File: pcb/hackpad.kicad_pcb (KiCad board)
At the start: 2 copper layers, 83.3 x 61.9 mm, 32 parts, among them U1 XIAO-RP2040-SMD

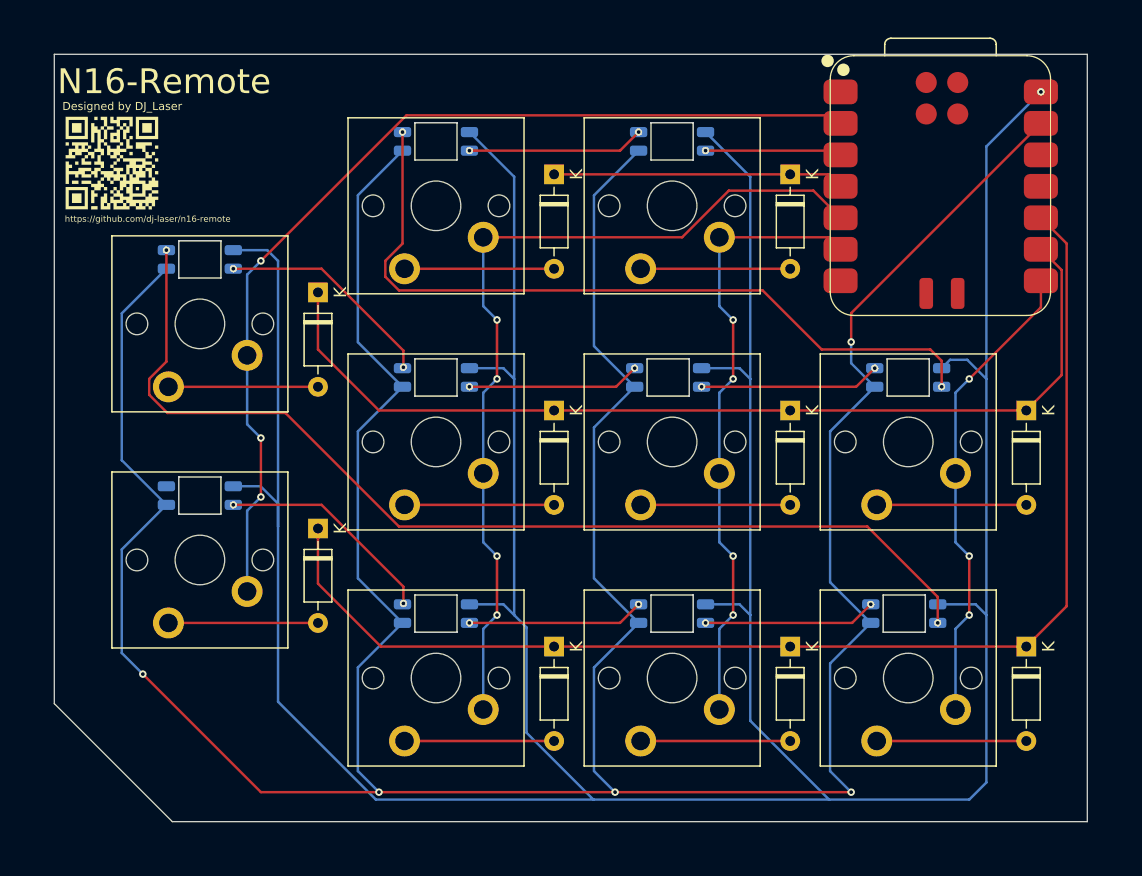
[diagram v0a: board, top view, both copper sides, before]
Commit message: i used the wrong data sheet to edit the footprint, changed the pcb to actually work :(
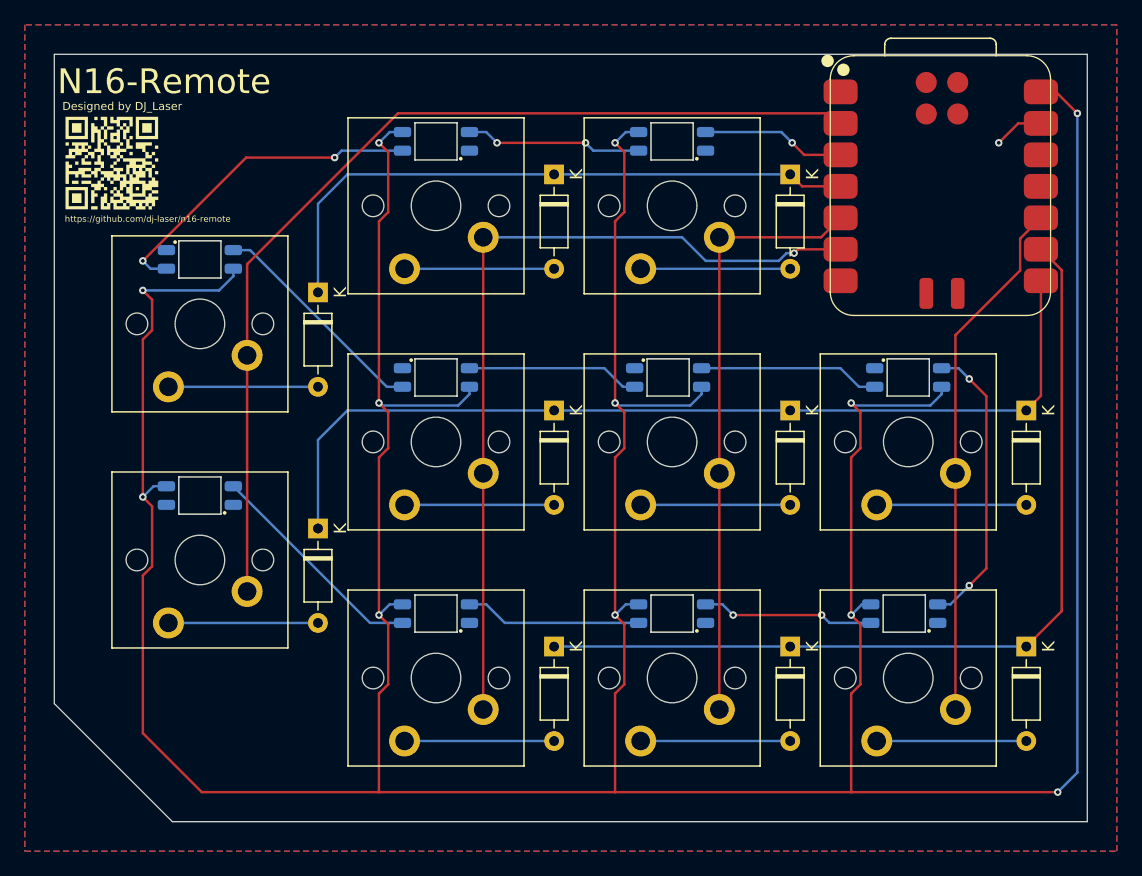
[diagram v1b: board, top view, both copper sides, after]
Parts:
- turned D_M2 to 0 degrees
- turned D_M3 to 0 degrees
- turned D_M4 to 0 degrees
- turned D_R1 to 0 degrees
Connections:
- D3 pad 1: Row 1 -> Row 0
- D7 pad 1: Row 2 -> Row 1
- D_B1 pad 1: Net-(D_B1-VDD) -> +5V
- D_B1 pad 2: GND -> Net-(D_B1-DOUT)
- D_B1 pad 3: Net-(D_B1-VSS) -> GND
- D_B1 pad 4: +5V -> Net-(D_B1-DIN)
- D_B2 pad 1: Net-(D_B1-VSS) -> +5V
- D_B2 pad 2: GND -> Net-(D_B1-DIN)
- D_B2 pad 3: Net-(D_B2-VSS) -> GND
- D_B2 pad 4: +5V -> Net-(D_B2-DIN)
- D_B3 pad 1: Net-(D_B2-VSS) -> +5V
- D_B3 pad 2: GND -> Net-(D_B2-DIN)
- D_B3 pad 3: Net-(D_B3-DIN) -> GND
- D_B3 pad 4: +5V -> Net-(D_B3-DIN)
- D_C1 pad 1: Net-(D_C1-DOUT) -> +5V
- D_C1 pad 2: GND -> Net-(D_C1-DOUT)
- D_C1 pad 3: Net-(D_C1-DIN) -> GND
- D_C1 pad 4: +5V -> Net-(D_C1-DIN)
- D_M1 pad 1: Net-(D_C1-DIN) -> +5V
- D_M1 pad 2: GND -> Net-(D_C1-DIN)
- D_M1 pad 3: RGB -> GND
- D_M1 pad 4: +5V -> RGB
- D_M2 pad 1: Net-(D_M2-VDD) -> +5V
- D_M2 pad 2: GND -> Net-(D_M2-DOUT)
- D_M2 pad 3: Net-(D_M2-VSS) -> GND
- D_M2 pad 4: +5V -> Net-(D_M2-DIN)
- D_M3 pad 1: Net-(D_M2-VSS) -> +5V
- D_M3 pad 2: GND -> Net-(D_M3-DOUT)
- D_M3 pad 3: Net-(D_M3-VSS) -> GND
- D_M3 pad 4: +5V -> Net-(D_M2-DOUT)
- D_M4 pad 1: Net-(D_M3-VSS) -> +5V
- D_M4 pad 2: GND -> Net-(D_B3-DIN)
- D_M4 pad 3: Net-(D_C1-DOUT) -> GND
- D_M4 pad 4: +5V -> Net-(D_M3-DOUT)
- D_R1 pad 1: Net-(D_B3-DIN) -> +5V
- D_R1 pad 2: GND -> Net-(D_M2-DIN)
- D_R1 pad 3: Net-(D_M2-VDD) -> GND
- D_R1 pad 4: +5V -> Net-(D_C1-DOUT)
- D_R2 pad 1: unconnected-(D_R2-DOUT-Pad1) -> +5V
- D_R2 pad 2: GND -> unconnected-(D_R2-DOUT-Pad2)
- D_R2 pad 3: Net-(D_B1-VDD) -> GND
- D_R2 pad 4: +5V -> Net-(D_B1-DOUT)
- U1 pad 10: Row 2 -> Col 3
- U1 pad 5: Col 1 -> Col 2
- U1 pad 6: Col 2 -> Col 1
- U1 pad 8: Col 3 -> Row 1
- U1 pad 9: Row 1 -> Row 2
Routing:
- net GND: track 284.6 -> 4.05 mm, vias 5 -> 1
- net Net-(D_B3-DIN): track 84.7 -> 23.6 mm
- net +5V: track 305.1 -> 359.3 mm, vias 1 -> 12
- net Net-(D_C1-DOUT): track 62.0 -> 26.8 mm
- net Row 2: track 100.5 -> 72.0 mm
- net Row 0: track 23.5 -> 50.7 mm
- net Net-(D_M2-DIN): track 0.00 -> 18.2 mm
- net Net-(D_B1-DOUT): track 0.00 -> 18.2 mm
- net Net-(D_M2-VDD): track 17.8 -> 0.00 mm, vias 2 -> 0
- net Net-(D_B1-VDD): track 17.8 -> 0.00 mm, vias 2 -> 0
- net Net-(D_M3-VSS): track 14.6 -> 0.00 mm, vias 2 -> 0
- net Net-(D_M3-DOUT): track 0.00 -> 14.6 mm
- net Net-(D_B1-VSS): track 14.3 -> 0.00 mm, vias 2 -> 0
- net Net-(D_B1-DIN): track 0.00 -> 14.3 mm
- net Net-(D_B2-DIN): track 0.00 -> 14.0 mm, vias 0 -> 2
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- added copper zone on B.Cu, net GND
- added copper zone on F.Cu, net GND

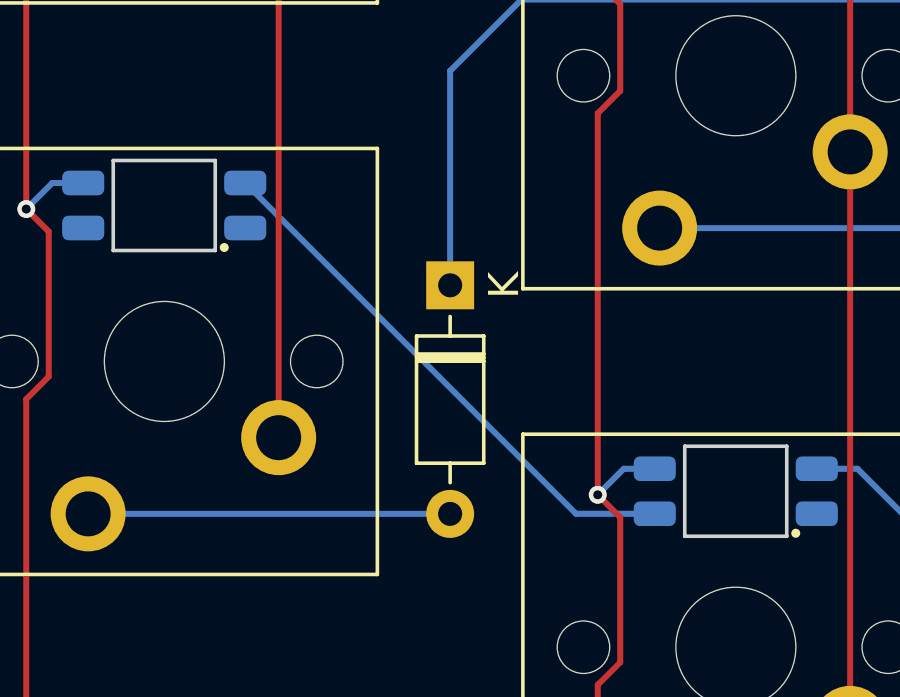
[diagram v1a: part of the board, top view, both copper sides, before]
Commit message: fix drc errors (by lowering clearance)
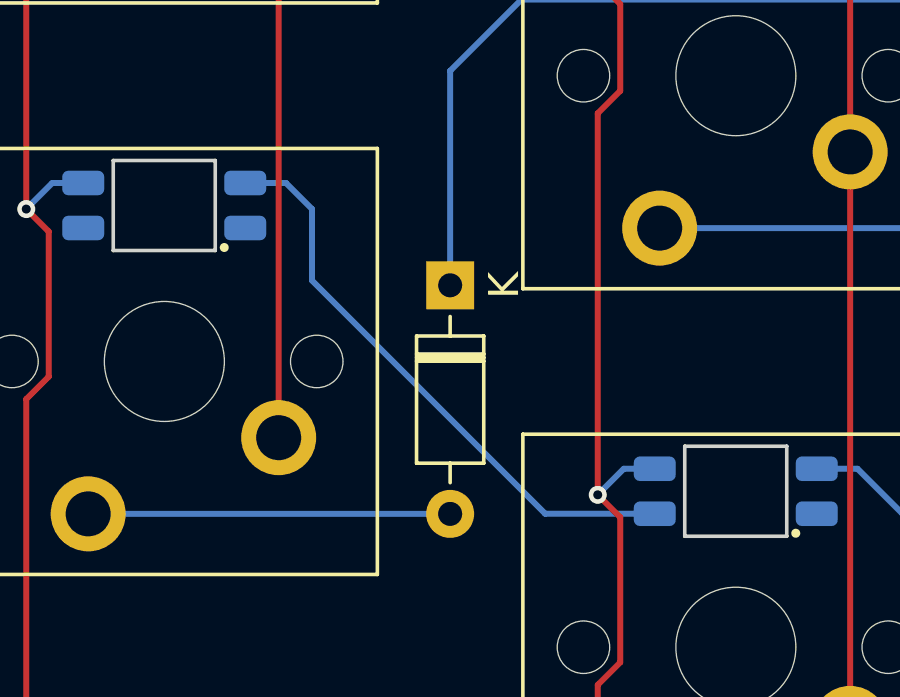
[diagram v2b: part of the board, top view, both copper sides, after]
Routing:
- net Net-(D_B1-DOUT): track 18.2 -> 19.6 mm
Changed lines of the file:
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@@
 	)
 	(segment
-		(start 59.05 93.5)
-		(end 56.425 93.5)
+		(start 47.625 85.725)
+		(end 47.625 83.34375)
 		(width 0.2)
 		(layer "B.Cu")
@@
 	)
 	(segment
-		(start 56.425 93.5)
+		(start 47.625 83.34375)
+		(end 46.75625 82.475)
+		(width 0.2)
+		(layer "B.Cu")
+		(net 30)
+	)
+	(segment
+		(start 55.4 93.5)
+		(end 47.625 85.725)
+		(width 0.2)
+		(layer "B.Cu")
+		(net 30)
+	)
+	(segment
+		(start 59.05 93.5)
+		(end 55.4 93.5)
+		(width 0.2)
+		(layer "B.Cu")
+		(net 30)
+	)
+	(segment
+		(start 46.75625 82.475)
 		(end 45.4 82.475)
 		(width 0.2)

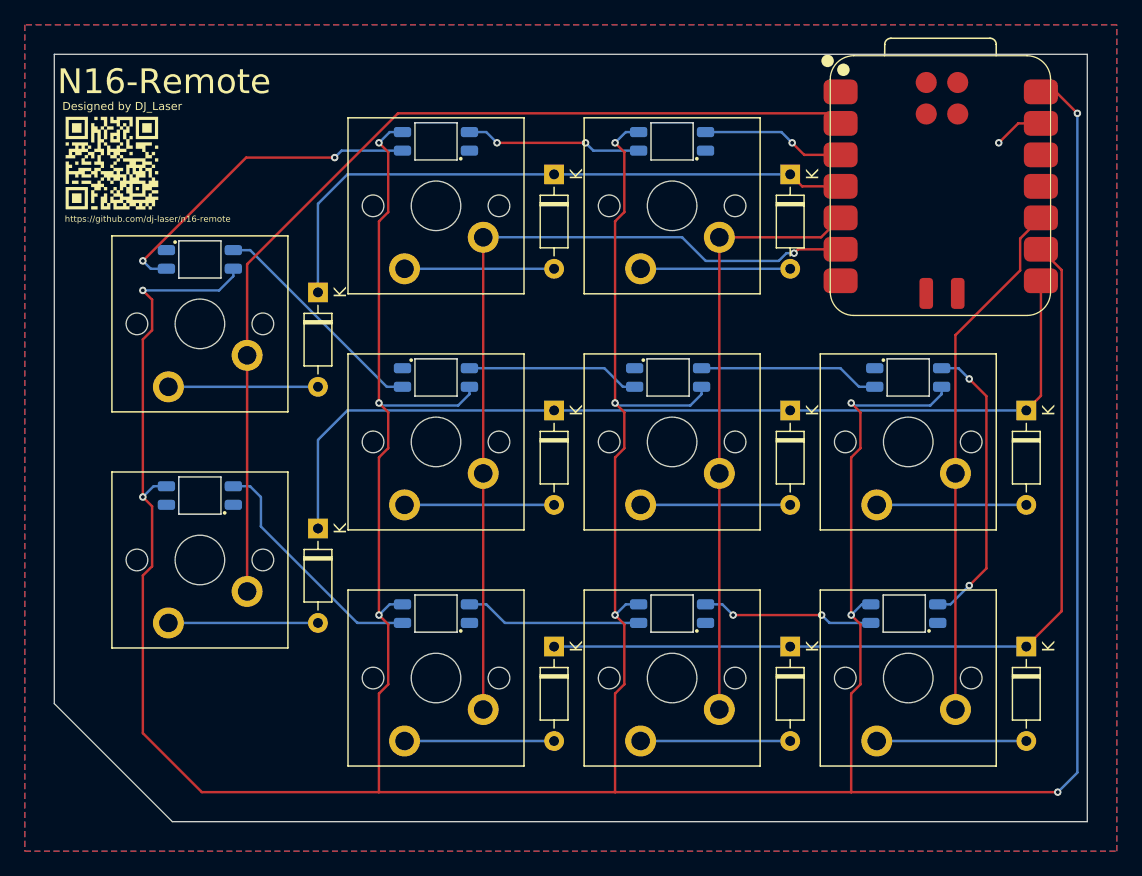
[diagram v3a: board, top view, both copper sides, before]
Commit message: add holes for mounting the case to the pcb
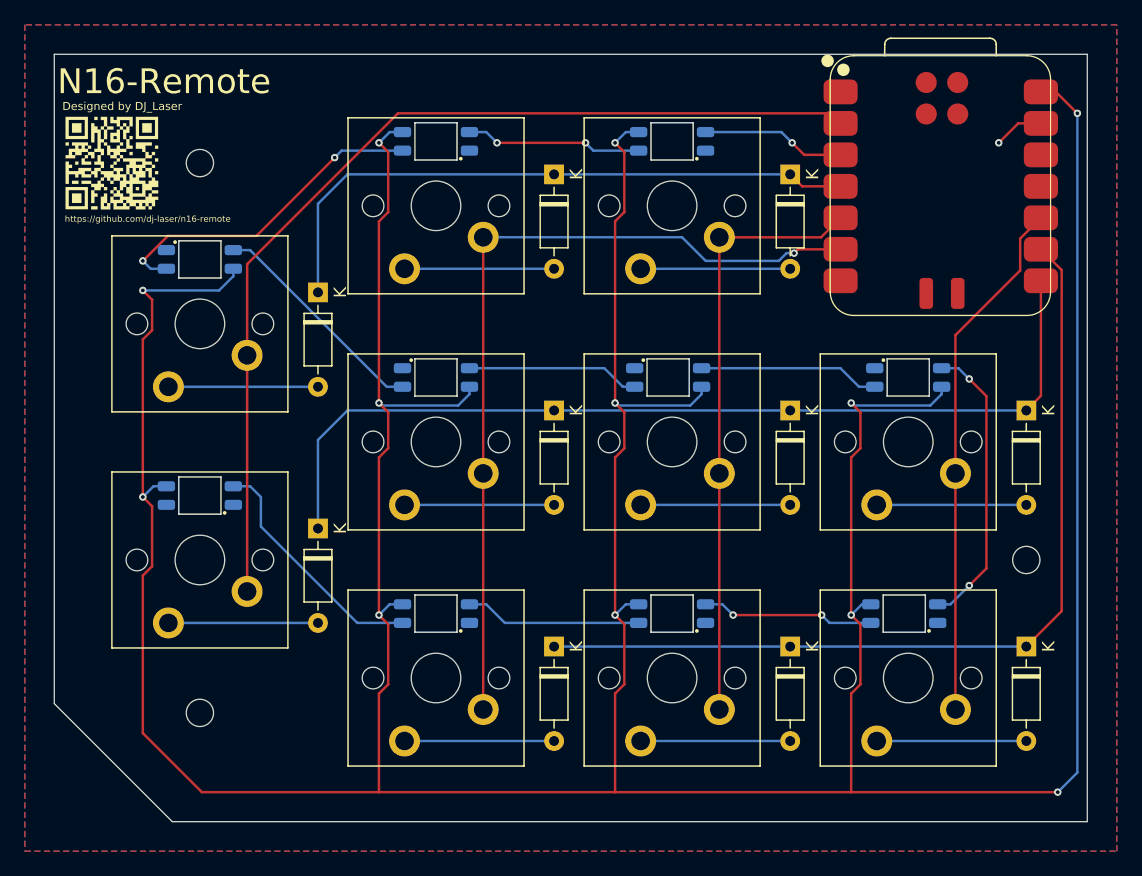
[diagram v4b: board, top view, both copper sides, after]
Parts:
- added REF**: MountingHole_2.2mm_M2, MountingHole:MountingHole_2.2mm_M2, F.Cu at (42.7, 100.8)
- added REF**: MountingHole_2.2mm_M2, MountingHole:MountingHole_2.2mm_M2, F.Cu at (109.4, 88.4)
- added REF**: MountingHole_2.2mm_M2, MountingHole:MountingHole_2.2mm_M2, F.Cu at (42.7, 56.4)

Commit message: remove backup gerbers from git
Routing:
- net +5V: track 359.3 -> 360.2 mm

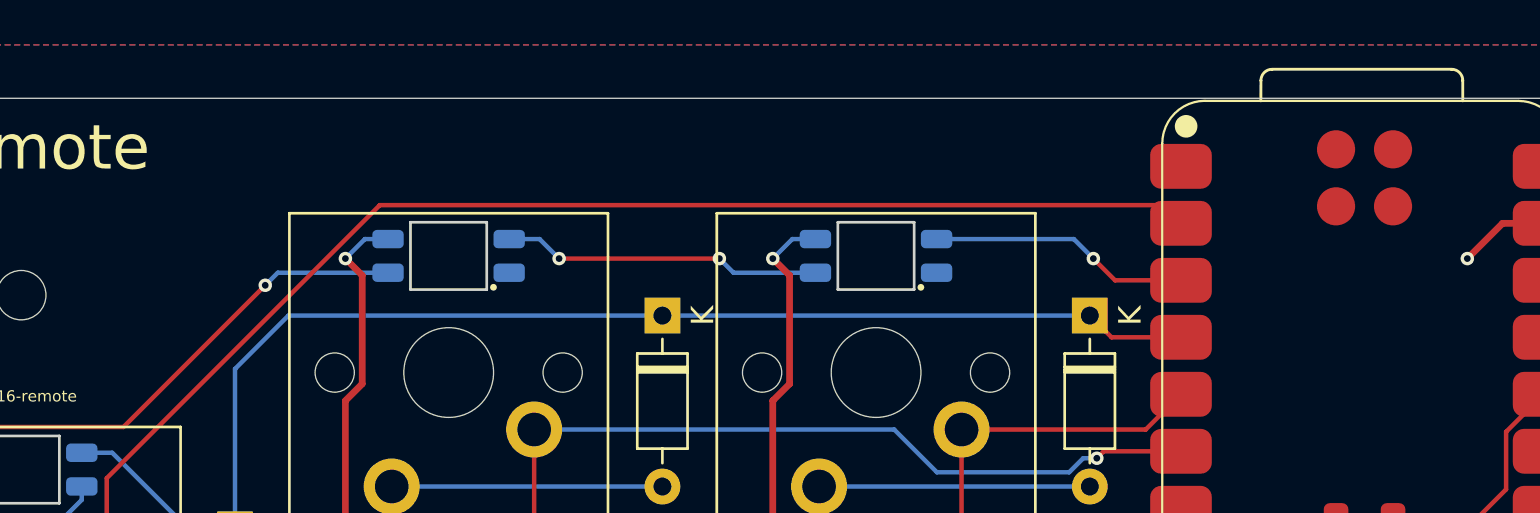
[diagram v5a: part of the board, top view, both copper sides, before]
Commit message: add holes to the smd debug pads
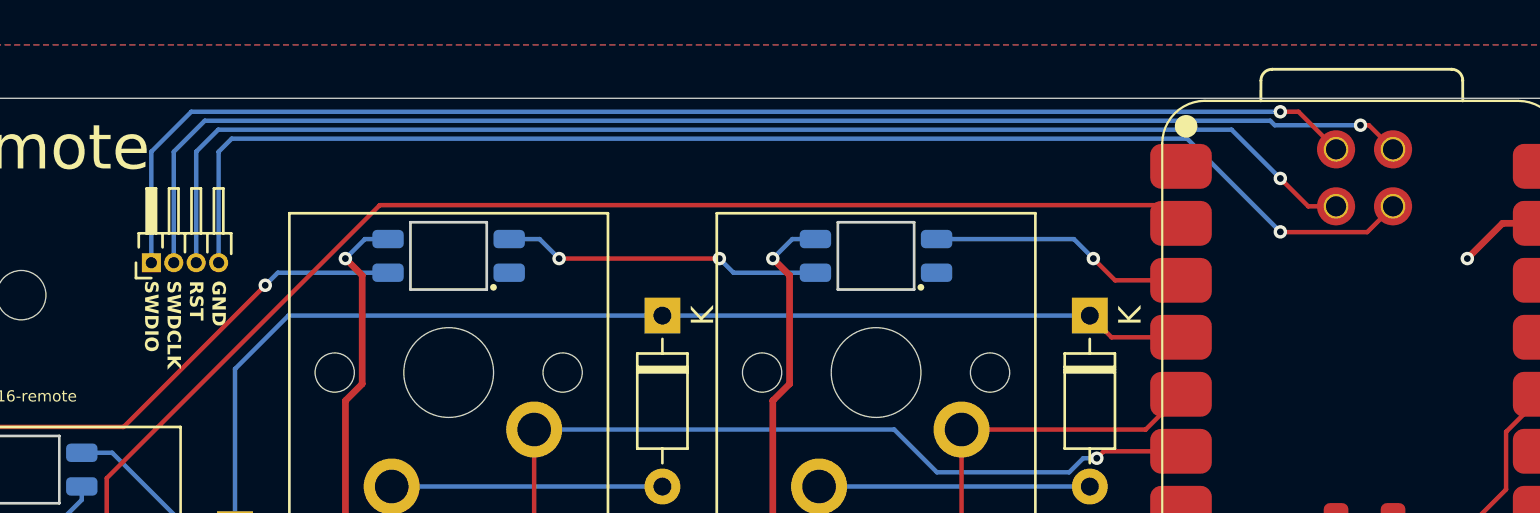
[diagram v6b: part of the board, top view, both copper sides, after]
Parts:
- added J1: Conn_01x04_Pin, Connector_PinHeader_1.00mm:PinHeader_1x04_P1.00mm_Horizontal, F.Cu at (48.5, 55.0)
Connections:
- U1 pad 17: unconnected-(U1-SWDIO-Pad17) -> Net-(J1-Pin_1)
- U1 pad 18: unconnected-(U1-SWDCLK-Pad18) -> Net-(J1-Pin_2)
- U1 pad 19: unconnected-(U1-RST-Pad19) -> Net-(J1-Pin_3)
- U1 pad 20: unconnected-(U1-GND-Pad20) -> Net-(J1-Pin_4)
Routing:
- net Net-(J1-Pin_2): track 0.00 -> 60.4 mm, vias 0 -> 1
- net Net-(J1-Pin_4): track 0.00 -> 59.7 mm, vias 0 -> 1
- net Net-(J1-Pin_1): track 0.00 -> 59.2 mm, vias 0 -> 1
- net Net-(J1-Pin_3): track 0.00 -> 57.6 mm, vias 0 -> 1
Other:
- board text added: "GND"
- board text added: "RST"
- board text added: "SWDCLK"
- board text added: "SWDIO"

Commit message: moar pcb
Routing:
- net +5V: track 360.2 -> 360.7 mm
- net Net-(J1-Pin_4): vias 1 -> 0
- net Net-(J1-Pin_3): vias 1 -> 0
- net Net-(J1-Pin_1): vias 1 -> 0
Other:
- board text added: "JLCJLCJLC"

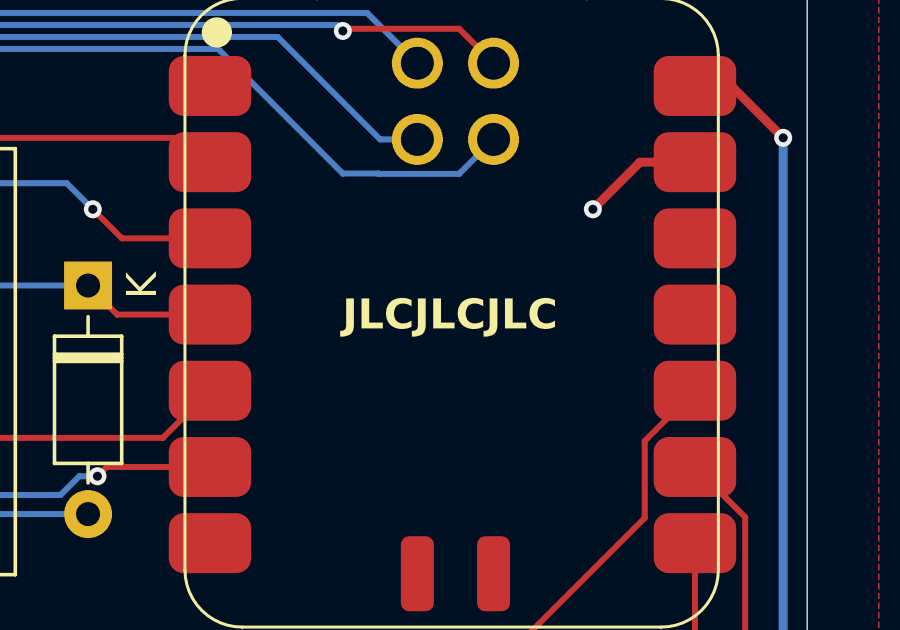
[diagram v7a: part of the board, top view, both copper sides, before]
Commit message: remove "jlcjlcjlc"
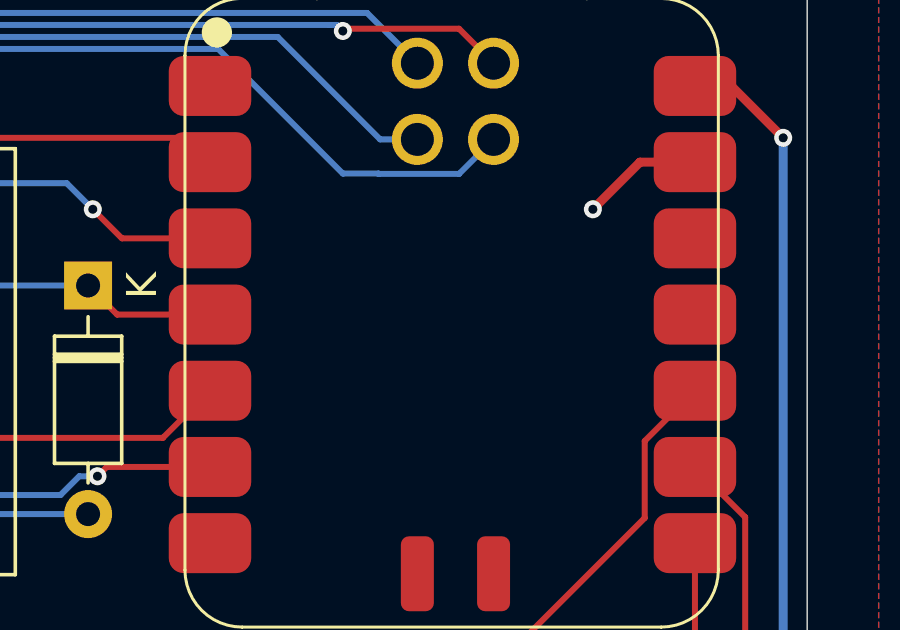
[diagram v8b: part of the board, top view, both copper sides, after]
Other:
- board text removed: "JLCJLCJLC"
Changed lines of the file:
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@@
-		)
-	)
-	(gr_text "JLCJLCJLC"
-		(at 102.39375 58.278 0)
-		(layer "F.SilkS")
-		(effects
-			(font
-				(size 1 1)
-				(thickness 0.2)
-				(bold yes)
-			)
 		)
 	)
